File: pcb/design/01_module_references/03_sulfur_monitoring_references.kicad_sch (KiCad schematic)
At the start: 12 parts, among them U1 SPI SD-CARD, U2 Anemometer, U3 Wind Direction, U4 Heltec WSL V3 JP

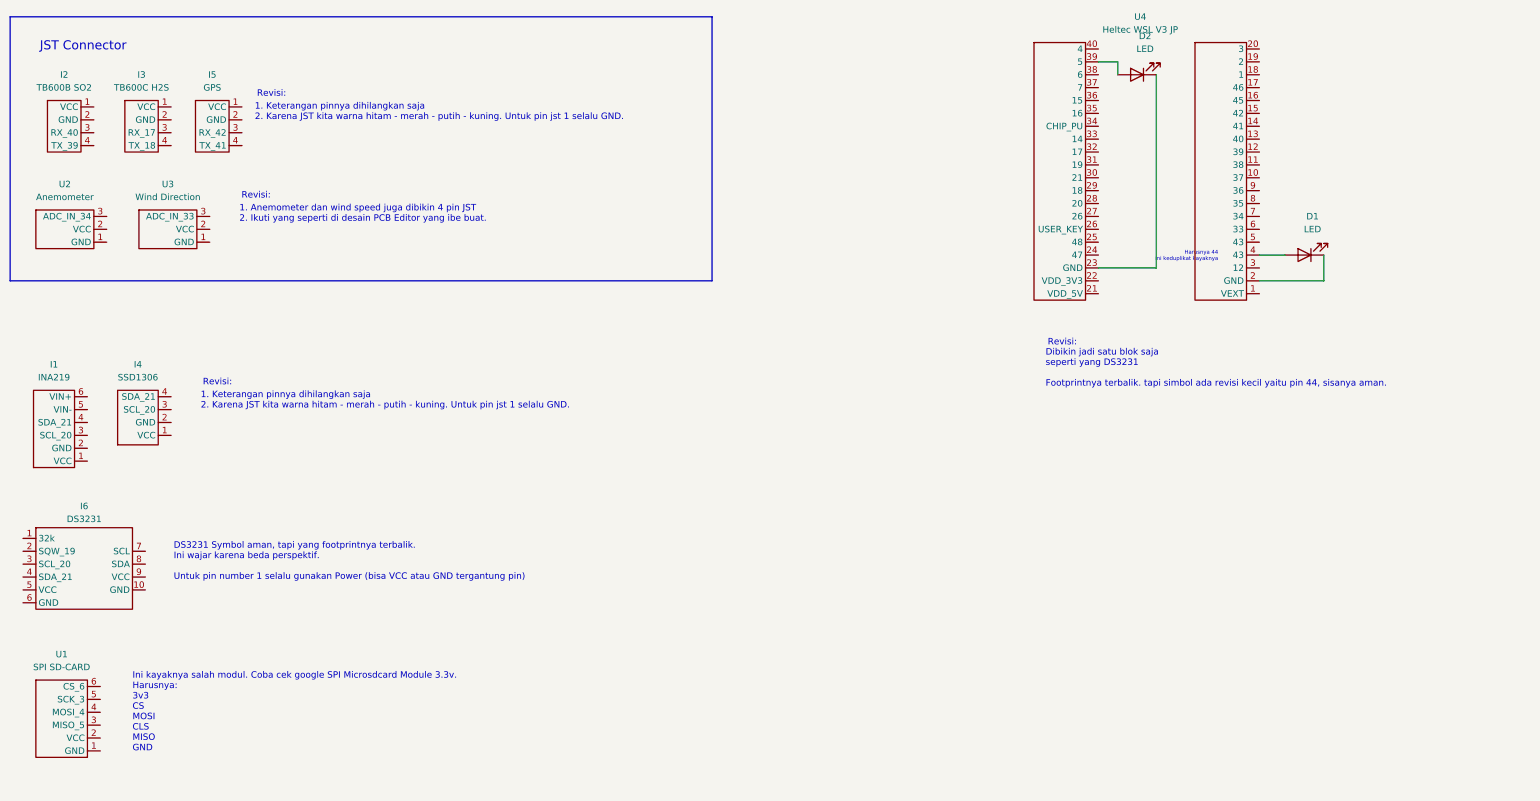
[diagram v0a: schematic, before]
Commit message: edit some footprint
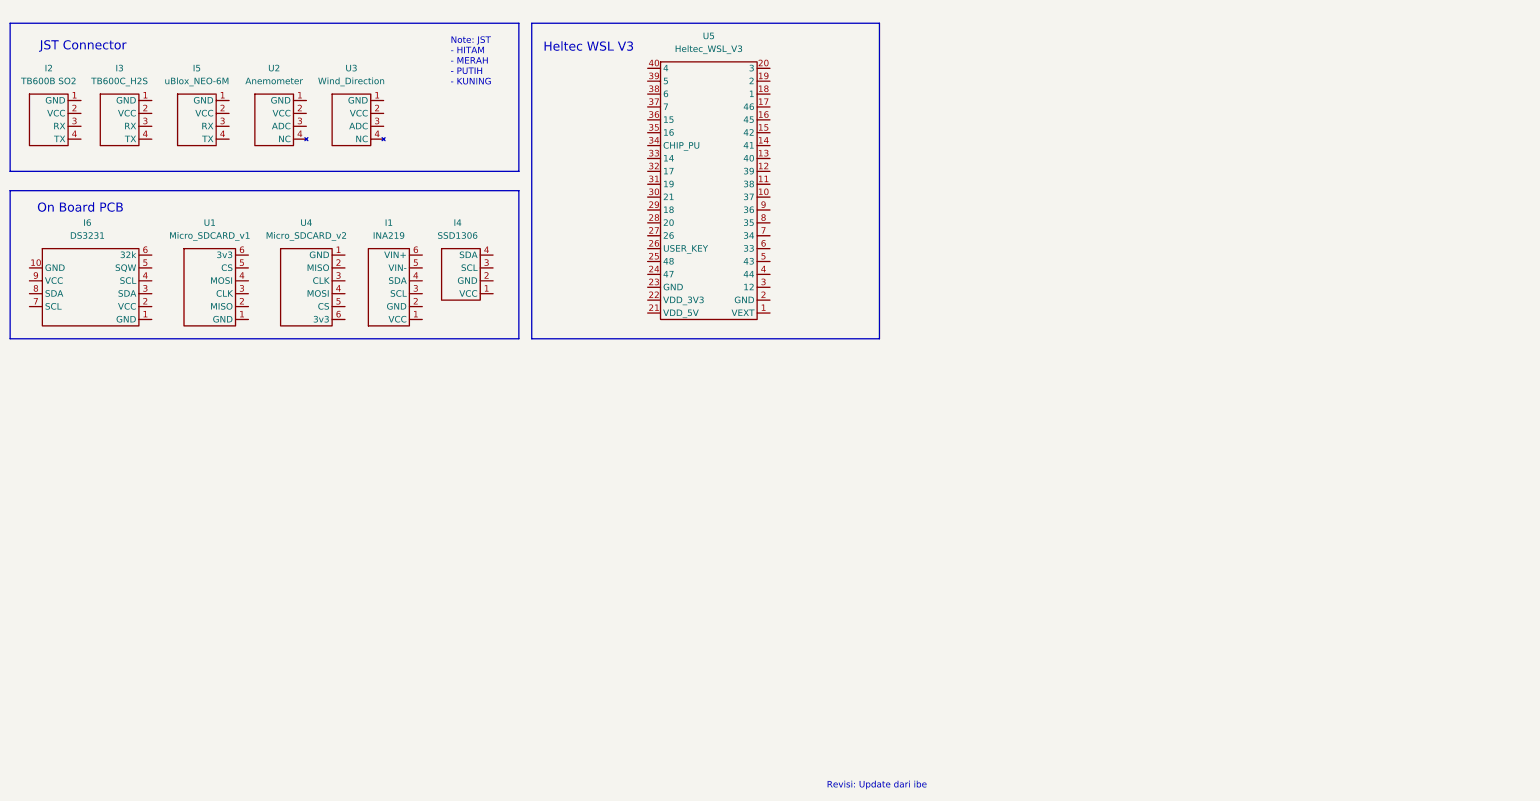
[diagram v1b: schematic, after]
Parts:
- removed D1, D2: LED, LED_THT:LED_D5.0mm, symbol Device:LED
- removed I2: TB600B SO2, Custom Board:TB600B, symbol Custom Board:TB600B
- removed I3: TB600C H2S, Custom Board:TB600C, symbol tb600c:TB600C
- removed I4: SSD1306​, Custom Board:SSD1306 On-board, symbol Custom Board:SSD1306​
- removed I5: GPS, Custom Board:GPS, symbol Custom Board:GPS
- removed U2: Anemometer, Custom Board:Anemometer, symbol Custom Board:Anemometer
- removed U3: Wind Direction, Custom Board:Wind Direction, symbol Custom Board:Wind Direction
- removed U4: Heltec WSL V3 JP, Custom Board:HELTEC WSL V3 JP, symbol wsl_v3:WSL_V3
- added I2: TB600B SO2, Custom Board:TB600B_SO2, symbol myCustom_STAS_RG:TB600B
- added I3: TB600C_H2S, Custom Board:TB600C_H2S, symbol myCustom_STAS_RG:TB600C
- added I4: SSD1306​, Custom Board:SSD1306_onBoard, symbol myCustom_STAS_RG:SSD1306​
- added I5: uBlox_NEO-6M, Custom Board:uBlox_NEO-6M, symbol myCustom_STAS_RG:GPS
- added U2: Anemometer, Custom Board:STASRG_Anemometer, symbol myCustom_STAS_RG:Anemometer
- added U3: Wind_Direction, Custom Board:STASRG_Wind_Dir, symbol myCustom_STAS_RG:Wind Direction
- added U4: Micro_SDCARD_v2, Custom Board:Micro_SDCARD_v2, symbol myCustom_STAS_RG:SPI SD Card_v2
- added U5: Heltec_WSL_V3, Custom Board:Heltec_WSL_V3_v1, symbol myCustom_STAS_RG:WSL_V3
- I1: symbol ina219:INA219 -> myCustom_STAS_RG:INA219
- I6: symbol Custom Board:RTC_DS3231​ -> myCustom_STAS_RG:RTC_DS3231​
- U1: value SPI SD-CARD -> Micro_SDCARD_v1; footprint Custom Board:SPI SD Card -> Custom Board:Micro_SDCARD_v1; symbol Custom Board:SPI SD Card -> myCustom_STAS_RG:SPI SD Card
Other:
- note added: "Heltec WSL V3"
- note added: "Note: JST - HITAM - MERAH - PUTIH - KUNING"
- note added: "On Board PCB"
- note added: "Revisi: Update dari ibe"
- note removed: "1. Anemometer dan wind speed juga dibikin 4 pin JST 2. Ikuti yang seperti di desain PCB Editor yang ibe buat."
- note removed: "1. Keterangan pinnya dihilangkan saja 2. Karena JST kita warna hitam - merah - putih - kuning. Untuk pin jst 1 selalu GND."
- note removed: "DS3231 Symbol aman, tapi yang footprintnya terbalik. Ini wajar karena beda perspektif. Untuk pin number 1 selalu gunakan Power (bisa VCC atau GND tergantung pin)"
- note removed: "Dibikin jadi satu blok saja seperti yang DS3231 Footprintnya terbalik. tapi simbol ada revisi kecil yaitu pin 44, sisanya aman."
- note removed: "Harusnya 44 ini keduplikat kayaknya"
- note removed: "Ini kayaknya salah modul. Coba cek google SPI Microsdcard Module 3.3v. Harusnya: 3v3 CS MOSI CLS MISO GND"
- note removed: "Revisi:"
- moved on the sheet: I1, I6, U1
